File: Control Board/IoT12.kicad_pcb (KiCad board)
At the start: 2 copper layers, 99.1 x 69.8 mm, 110 parts, among them J10 USB_B_Micro, J11 Conn_ARM_JTAG_SWD_10, J9 Conn_ARM_JTAG_SWD_10, Q1 MMBT2222, Q2 MMBT2222, Q3 AOD403, SW1 Rotary encoder EC11 Plum 15mm, SW2 SW_Push, U1 ATSAMD21G, U2 ADS1115IDGS, U3 INA826AID, U4 INA826AID, U5 LM2596S-ADJ, U6 AT24C32, Y1 32768Hz

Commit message: Changed license to permissive.
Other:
- board text added: "https://github.com/atoomnetmarc/IoT12-hardware Apache License, Version 2.0"
- board text removed: "https://github.com/atoomnetmarc/IoT12-hardware License: Creative Commons Attribution-NonCommercial 3.0 Unported"

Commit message: Soldered V2.0 pcb.
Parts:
- C1, C2: value 6.7pF -> 6.8pF
- C50: value 4.7uF -> 10uF
- U1: value ATSAMD21G -> ATSAMD21G18A-AU

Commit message: Start of V2.1 PCB.
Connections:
- U1 pad 13: ESP32_SCL -> ESP32_SDA
- U1 pad 14: ESP32_SDA -> ESP32_SCL
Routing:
- net ESP32_SDA: track 27.9 -> 28.6 mm
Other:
- board text added: "IoT12, 2021-03-07, V2.1 https://atoomnet.net"
- board text removed: "IoT12, 2021-02-22, V2.0 https://atoomnet.net"

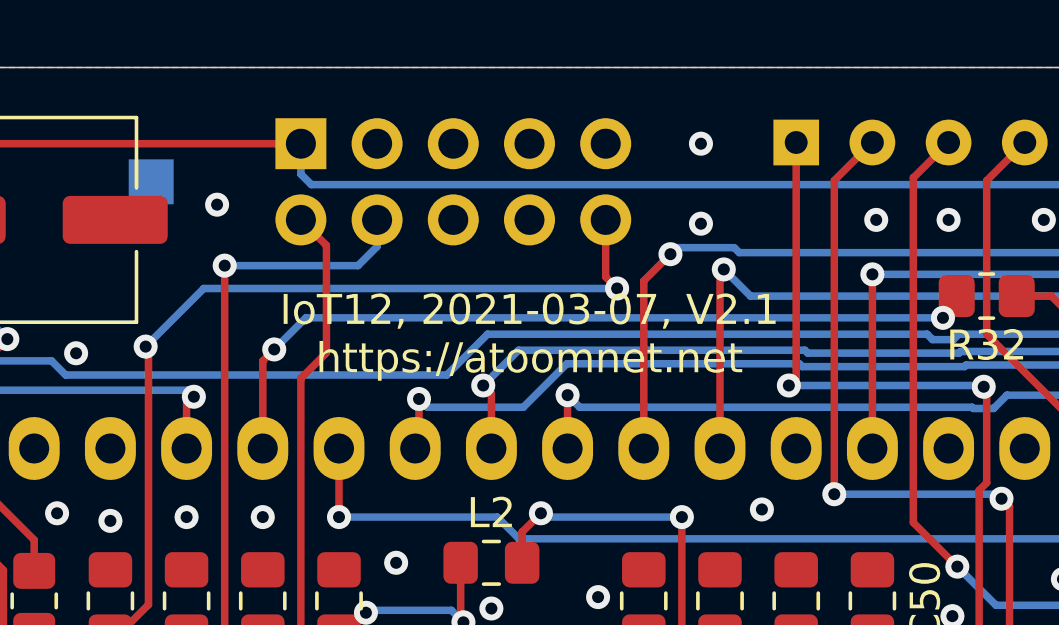
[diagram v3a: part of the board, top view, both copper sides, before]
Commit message: Added SDA2/SCL2 labels on SAMD21.
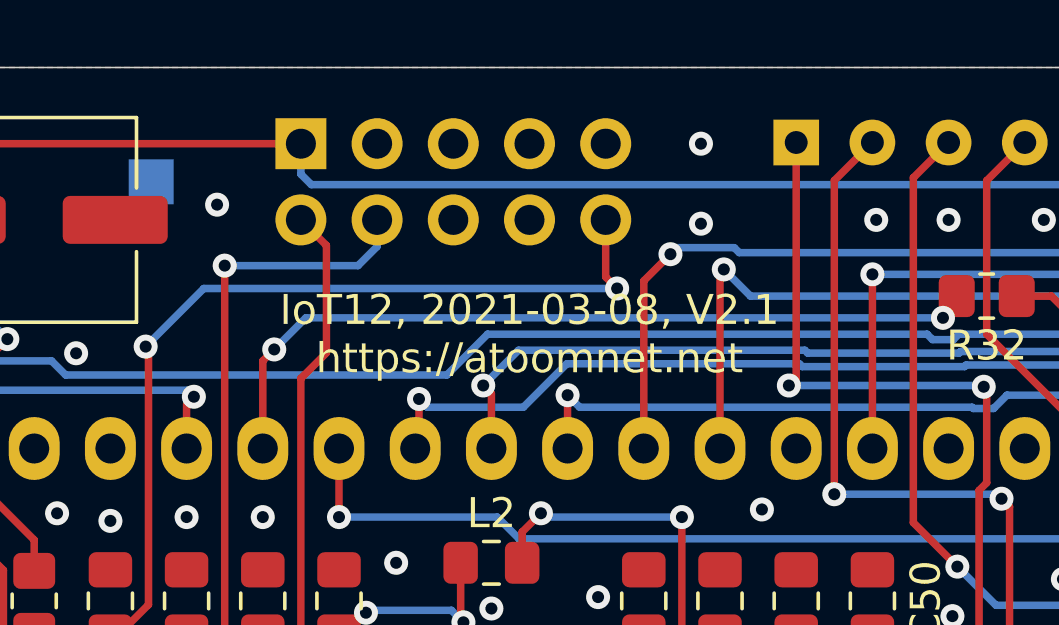
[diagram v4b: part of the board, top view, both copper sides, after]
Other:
- board text added: "IoT12, 2021-03-08, V2.1 https://atoomnet.net"
- board text removed: "IoT12, 2021-03-07, V2.1 https://atoomnet.net"

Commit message: Samd21 D2, D4 where swapped in symbol. No pcb change.
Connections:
- net PWM_HEAT renamed HEAT_PWM

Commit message: More erratum.
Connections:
- U1 pad 31: HEAT_SCL -> HEAT_SDA
- U1 pad 32: HEAT_SDA -> HEAT_SCL
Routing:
- net HEAT_SCL: track 58.6 -> 59.2 mm
